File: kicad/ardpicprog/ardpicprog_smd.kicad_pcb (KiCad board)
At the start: 2 copper layers, 69.2 x 53.9 mm, 37 parts, among them P1 CONN_01X06, P2 CONN_01X02, Q1 BC548, SW1 SW_PUSH, U1 PIC16F627, U2 MC34063, U3 LM78L12ACZ

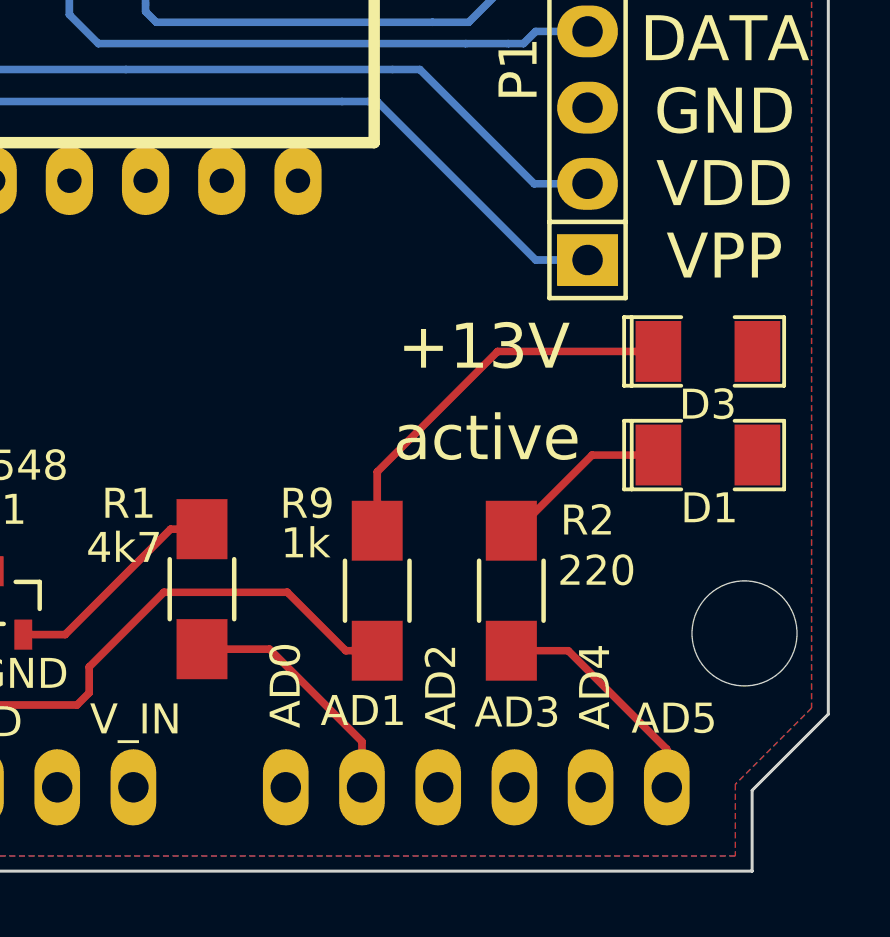
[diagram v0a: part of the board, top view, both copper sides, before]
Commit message: VDD d2 connection fix
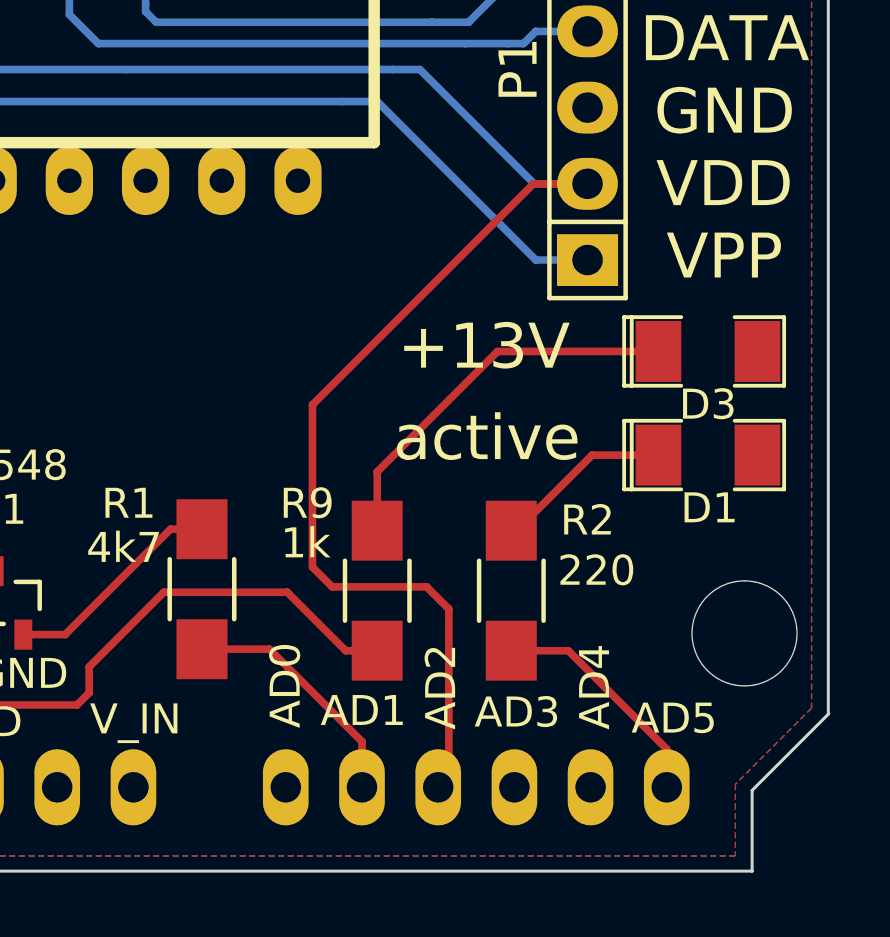
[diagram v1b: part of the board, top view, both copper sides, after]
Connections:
- SHIELD1 pad AD2: (no net) -> VDD(D2)
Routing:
- net VDD(D2): track 49.8 -> 78.6 mm
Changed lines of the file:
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@@
-(kicad_pcb (version 4) (host pcbnew "(2014-jul-16 BZR unknown)-product")
+(kicad_pcb (version 4) (host pcbnew 0.201506232253+5814~23~ubuntu14.04.1-product)
   (general
-    (links 73)
+    (links 74)
     (no_connects 0)
     (area 129.286799 76.099199 198.576401 130.148801)
     (thickness 1.6)
     (drawings 34)
-    (tracks 234)
+    (tracks 242)
     (zones 0)
     (modules 37)
@@
     (pad AD1 thru_hole oval (at 53.34 -2.54 90) (size 2.54 1.524) (drill 1.016) (layers *.Cu *.Mask F.SilkS)
       (net 19 "MCLR(A1)"))
-    (pad AD2 thru_hole oval (at 55.88 -2.54 90) (size 2.54 1.524) (drill 1.016) (layers *.Cu *.Mask F.SilkS))
+    (pad AD2 thru_hole oval (at 55.88 -2.54 90) (size 2.54 1.524) (drill 1.016) (layers *.Cu *.Mask F.SilkS)
+      (net 1 "VDD(D2)"))
     (pad V_IN thru_hole oval (at 45.72 -2.54 90) (size 2.54 1.524) (drill 1.016) (layers *.Cu *.Mask F.SilkS))
     (pad GND2 thru_hole oval (at 43.18 -2.54 90) (size 2.54 1.524) (drill 1.016) (layers *.Cu *.Mask F.SilkS)
@@
   (gr_line (start 194.5132 76.1492) (end 195.9864 77.6224) (angle 90) (layer Edge.Cuts) (width 0.1))
   (gr_line (start 130.286 76.1492) (end 194.5132 76.1492) (angle 90) (layer Edge.Cuts) (width 0.1))
+  (segment (start 190.5 107.188) (end 188.6966 107.188) (width 0.254) (layer F.Cu) (net 1) (status 400000))
+  (segment (start 185.8772 121.3612) (end 185.8772 126.9492) (width 0.254) (layer F.Cu) (net 1) (status 800000))
+  (segment (start 185.1406 120.6246) (end 185.8772 121.3612) (width 0.254) (layer F.Cu) (net 1))
+  (segment (start 181.991 120.6246) (end 185.1406 120.6246) (width 0.254) (layer F.Cu) (net 1))
+  (segment (start 181.3306 119.9642) (end 181.991 120.6246) (width 0.254) (layer F.Cu) (net 1))
+  (segment (start 181.3306 114.554) (end 181.3306 119.9642) (width 0.254) (layer F.Cu) (net 1))
+  (segment (start 188.6966 107.188) (end 181.3306 114.554) (width 0.254) (layer F.Cu) (net 1))
+  (segment (start 185.8772 126.9492) (end 185.5216 127.3048) (width 0.254) (layer F.Cu) (net 1) (status C00000))
   (segment (start 145.0528 98.9584) (end 145.0528 99.79) (width 0.254) (layer F.Cu) (net 1))
   (segment (start 147.8788 103.378) (end 149.1488 103.378) (width 0.254) (layer F.Cu) (net 1))

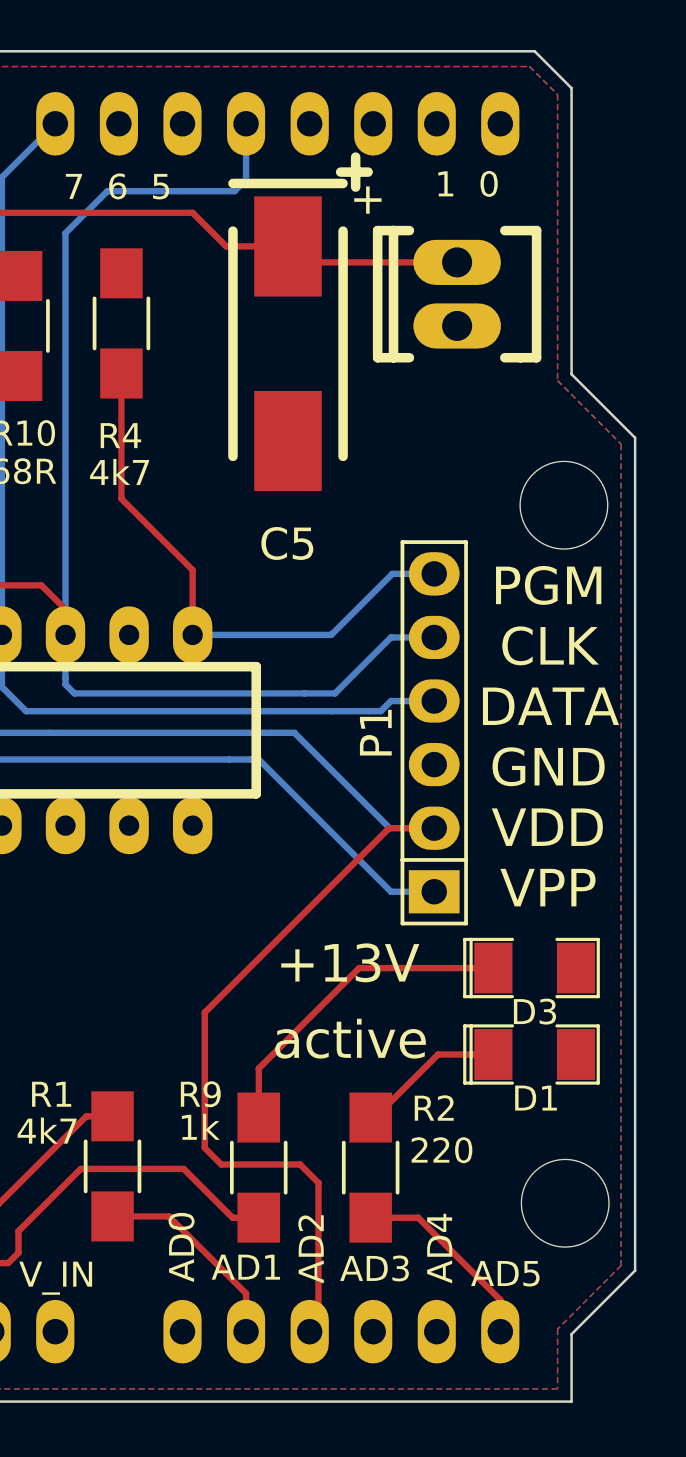
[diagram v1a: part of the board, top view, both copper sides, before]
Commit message: VDD d2 connection fix
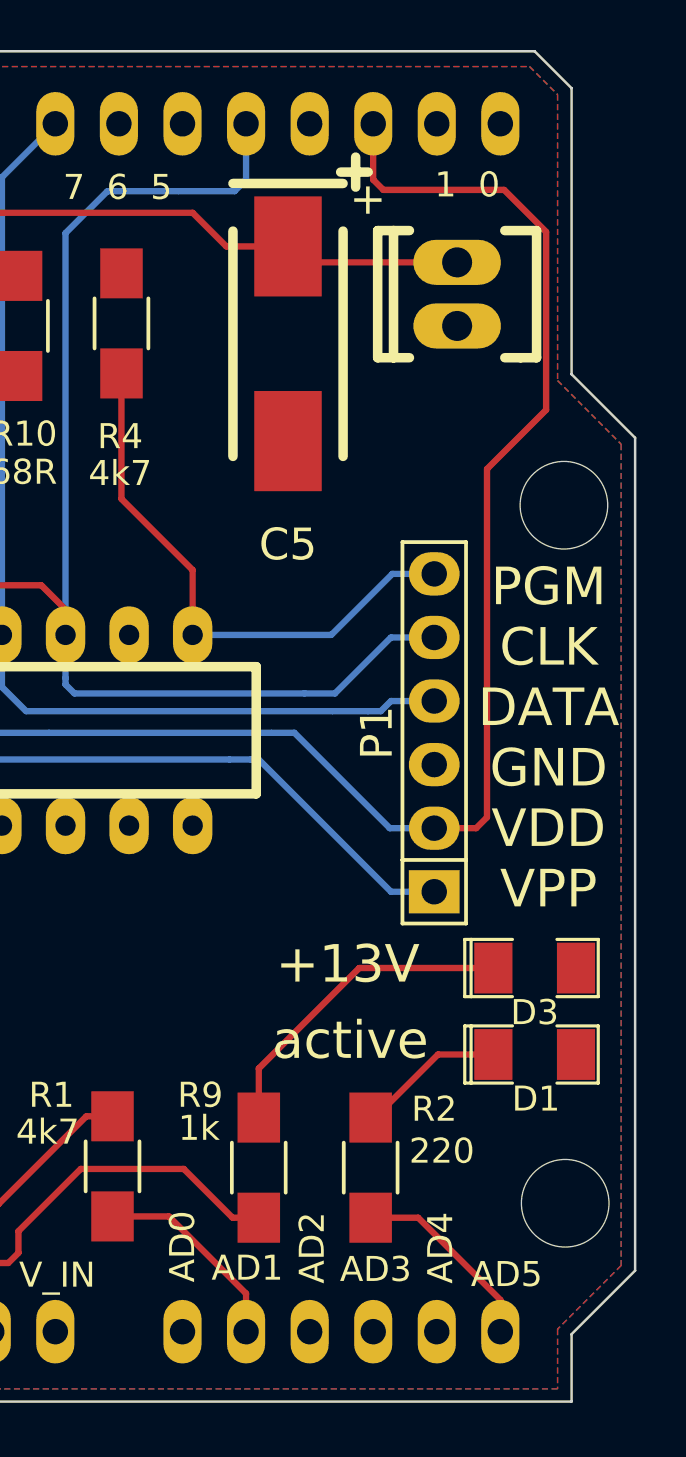
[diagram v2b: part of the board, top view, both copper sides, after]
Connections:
- SHIELD1 pad 2: (no net) -> VDD(D2)
- SHIELD1 pad AD2: VDD(D2) -> (no net)
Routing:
- net VDD(D2): track 78.6 -> 86.5 mm
- net (no net): track 0.00 -> 0.50 mm
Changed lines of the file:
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@@
     (thickness 1.6)
     (drawings 34)
-    (tracks 242)
+    (tracks 244)
     (zones 0)
     (modules 37)
@@
     (pad AD1 thru_hole oval (at 53.34 -2.54 90) (size 2.54 1.524) (drill 1.016) (layers *.Cu *.Mask F.SilkS)
       (net 19 "MCLR(A1)"))
-    (pad AD2 thru_hole oval (at 55.88 -2.54 90) (size 2.54 1.524) (drill 1.016) (layers *.Cu *.Mask F.SilkS)
-      (net 1 "VDD(D2)"))
+    (pad AD2 thru_hole oval (at 55.88 -2.54 90) (size 2.54 1.524) (drill 1.016) (layers *.Cu *.Mask F.SilkS))
     (pad V_IN thru_hole oval (at 45.72 -2.54 90) (size 2.54 1.524) (drill 1.016) (layers *.Cu *.Mask F.SilkS))
     (pad GND2 thru_hole oval (at 43.18 -2.54 90) (size 2.54 1.524) (drill 1.016) (layers *.Cu *.Mask F.SilkS)
@@
     (pad 0 thru_hole oval (at 63.5 -50.8 90) (size 2.54 1.524) (drill 1.016) (layers *.Cu *.Mask F.SilkS))
     (pad 1 thru_hole oval (at 60.96 -50.8 90) (size 2.54 1.524) (drill 1.016) (layers *.Cu *.Mask F.SilkS))
-    (pad 2 thru_hole oval (at 58.42 -50.8 90) (size 2.54 1.524) (drill 1.016) (layers *.Cu *.Mask F.SilkS))
+    (pad 2 thru_hole oval (at 58.42 -50.8 90) (size 2.54 1.524) (drill 1.016) (layers *.Cu *.Mask F.SilkS)
+      (net 1 "VDD(D2)"))
     (pad 3 thru_hole oval (at 55.88 -50.8 90) (size 2.54 1.524) (drill 1.016) (layers *.Cu *.Mask F.SilkS))
     (pad 4 thru_hole oval (at 53.34 -50.8 90) (size 2.54 1.524) (drill 1.016) (layers *.Cu *.Mask F.SilkS)
@@
   (gr_line (start 194.5132 76.1492) (end 195.9864 77.6224) (angle 90) (layer Edge.Cuts) (width 0.1))
   (gr_line (start 130.286 76.1492) (end 194.5132 76.1492) (angle 90) (layer Edge.Cuts) (width 0.1))
-  (segment (start 190.5 107.188) (end 188.6966 107.188) (width 0.254) (layer F.Cu) (net 1) (status 400000))
-  (segment (start 185.8772 121.3612) (end 185.8772 126.9492) (width 0.254) (layer F.Cu) (net 1) (status 800000))
-  (segment (start 185.1406 120.6246) (end 185.8772 121.3612) (width 0.254) (layer F.Cu) (net 1))
-  (segment (start 181.991 120.6246) (end 185.1406 120.6246) (width 0.254) (layer F.Cu) (net 1))
-  (segment (start 181.3306 119.9642) (end 181.991 120.6246) (width 0.254) (layer F.Cu) (net 1))
-  (segment (start 181.3306 114.554) (end 181.3306 119.9642) (width 0.254) (layer F.Cu) (net 1))
-  (segment (start 188.6966 107.188) (end 181.3306 114.554) (width 0.254) (layer F.Cu) (net 1))
-  (segment (start 185.8772 126.9492) (end 185.5216 127.3048) (width 0.254) (layer F.Cu) (net 1) (status C00000))
+  (segment (start 185.8772 126.9492) (end 185.5216 127.3048) (width 0.254) (layer F.Cu) (net 0))
+  (segment (start 190.5 107.188) (end 192.1764 107.188) (width 0.254) (layer F.Cu) (net 1) (status 400000))
+  (segment (start 188.0616 81.28) (end 188.0616 79.0448) (width 0.254) (layer F.Cu) (net 1) (status 800000))
+  (segment (start 188.468 81.6864) (end 188.0616 81.28) (width 0.254) (layer F.Cu) (net 1))
+  (segment (start 193.294 81.6864) (end 188.468 81.6864) (width 0.254) (layer F.Cu) (net 1))
+  (segment (start 194.9704 83.3628) (end 193.294 81.6864) (width 0.254) (layer F.Cu) (net 1))
+  (segment (start 194.9704 90.4748) (end 194.9704 83.3628) (width 0.254) (layer F.Cu) (net 1))
+  (segment (start 192.6082 92.837) (end 194.9704 90.4748) (width 0.254) (layer F.Cu) (net 1))
+  (segment (start 192.6082 106.7562) (end 192.6082 92.837) (width 0.254) (layer F.Cu) (net 1))
+  (segment (start 192.1764 107.188) (end 192.6082 106.7562) (width 0.254) (layer F.Cu) (net 1))
   (segment (start 145.0528 98.9584) (end 145.0528 99.79) (width 0.254) (layer F.Cu) (net 1))
   (segment (start 147.8788 103.378) (end 149.1488 103.378) (width 0.254) (layer F.Cu) (net 1))

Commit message: updates
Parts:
- moved R5 12.5 mm to (134.8, 112.3), turned to 0 degrees
- moved R8 7.83 mm to (142.7, 115.4), turned to 180 degrees
- moved C2 7.43 mm to (142.5, 119.3)
- moved R7 6.59 mm to (134.7, 119.3), turned to 0 degrees
- moved D4 1.43 mm to (153.3, 121.3), turned to 0 degrees
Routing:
- net Net-(R7-Pad1): track 33.2 -> 21.2 mm
- net Net-(L1-Pad2): track 42.1 -> 36.1 mm
- net 13V: track 73.8 -> 69.3 mm
- net Net-(C4-Pad1): track 41.7 -> 45.2 mm
- net 5V: track 55.0 -> 52.7 mm
- net GND: track 0.00 -> 0.84 mm
